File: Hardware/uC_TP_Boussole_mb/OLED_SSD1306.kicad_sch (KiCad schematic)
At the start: 2 parts, among them J6 Conn_01x04

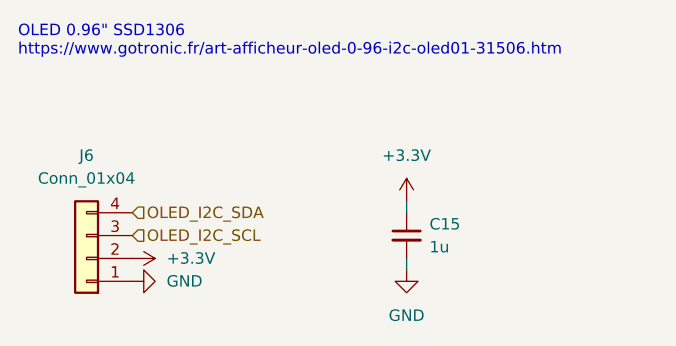
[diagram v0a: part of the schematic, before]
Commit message: starting pin out nucleo
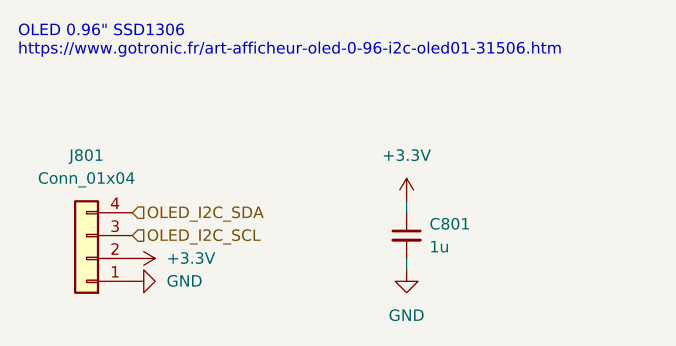
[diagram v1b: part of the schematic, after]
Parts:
- C801: renamed from C15; footprint (none) -> Capacitor_SMD:C_0402_1005Metric
- J801: renamed from J6; footprint (none) -> Connector_PinSocket_2.54mm:PinSocket_1x04_P2.54mm_Vertical
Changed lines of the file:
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@@
 		(dnp no)
 		(fields_autoplaced yes)
-		(property "Reference" "#PWR048"
+		(property "Reference" "#PWR0801"
 			(at 34.29 46.99 0)
 			(effects
@@
 			(project "uC_TP_Boussole_mb"
 				(path "/2e9feef3-d2ce-488a-99fa-e1de5099ffc3/51dbfd4b-530d-4bfc-b216-7850cc622368"
-					(reference "#PWR048")
+					(reference "#PWR0801")
 					(unit 1)
 				)
@@
 		(dnp no)
 		(fields_autoplaced yes)
-		(property "Reference" "#PWR051"
+		(property "Reference" "#PWR0804"
 			(at 68.58 54.61 0)
 			(effects
@@
 			(project "uC_TP_Boussole_mb"
 				(path "/2e9feef3-d2ce-488a-99fa-e1de5099ffc3/51dbfd4b-530d-4bfc-b216-7850cc622368"
-					(reference "#PWR051")
+					(reference "#PWR0804")
 					(unit 1)
 				)
@@
 		(dnp no)
 		(fields_autoplaced yes)
-		(property "Reference" "#PWR050"
+		(property "Reference" "#PWR0803"
 			(at 68.58 44.45 0)
 			(effects
@@
 			(project "uC_TP_Boussole_mb"
 				(path "/2e9feef3-d2ce-488a-99fa-e1de5099ffc3/51dbfd4b-530d-4bfc-b216-7850cc622368"
-					(reference "#PWR050")
+					(reference "#PWR0803")
 					(unit 1)
 				)
@@
 		(dnp no)
 		(fields_autoplaced yes)
-		(property "Reference" "C15"
+		(property "Reference" "C801"
 			(at 71.12 43.1862 0)
 			(effects
@@
 			)
 		)
-		(property "Footprint" ""
+		(property "Footprint" "Capacitor_SMD:C_0402_1005Metric"
 			(at 68.58 44.45 0)
 			(effects
@@
 			(project "uC_TP_Boussole_mb"
 				(path "/2e9feef3-d2ce-488a-99fa-e1de5099ffc3/51dbfd4b-530d-4bfc-b216-7850cc622368"
-					(reference "C15")
+					(reference "C801")
 					(unit 1)
 				)
@@
 		(dnp no)
 		(fields_autoplaced yes)
-		(property "Reference" "#PWR047"
+		(property "Reference" "#PWR0802"
 			(at 44.45 49.53 0)
 			(effects
@@
 			(project "uC_TP_Boussole_mb"
 				(path "/2e9feef3-d2ce-488a-99fa-e1de5099ffc3/51dbfd4b-530d-4bfc-b216-7850cc622368"
-					(reference "#PWR047")
+					(reference "#PWR0802")
 					(unit 1)
 				)
@@
 		(dnp no)
 		(fields_autoplaced yes)
-		(property "Reference" "J6"
+		(property "Reference" "J801"
 			(at 33.02 35.56 0)
 			(effects
@@
 			)
 		)
-		(property "Footprint" ""
+		(property "Footprint" "Connector_PinSocket_2.54mm:PinSocket_1x04_P2.54mm_Vertical"
 			(at 33.02 46.99 0)
 			(effects
@@
 			(project "uC_TP_Boussole_mb"
 				(path "/2e9feef3-d2ce-488a-99fa-e1de5099ffc3/51dbfd4b-530d-4bfc-b216-7850cc622368"
-					(reference "J6")
-					(unit 1)
-				)
+					(reference "J801")
+					(unit 1)
+				)

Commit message: ddd
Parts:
- added R801, R802: 1k, Resistor_SMD:R_0402_1005Metric, symbol Device:R_Small
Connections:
- net +3.3V: now also R801.2, R802.2
- net OLED_I2C_SCL: now also R801.1
- net OLED_I2C_SDA: now also R802.1
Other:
- note added: "Pull-up for I2C if it's not on OLED Screen"

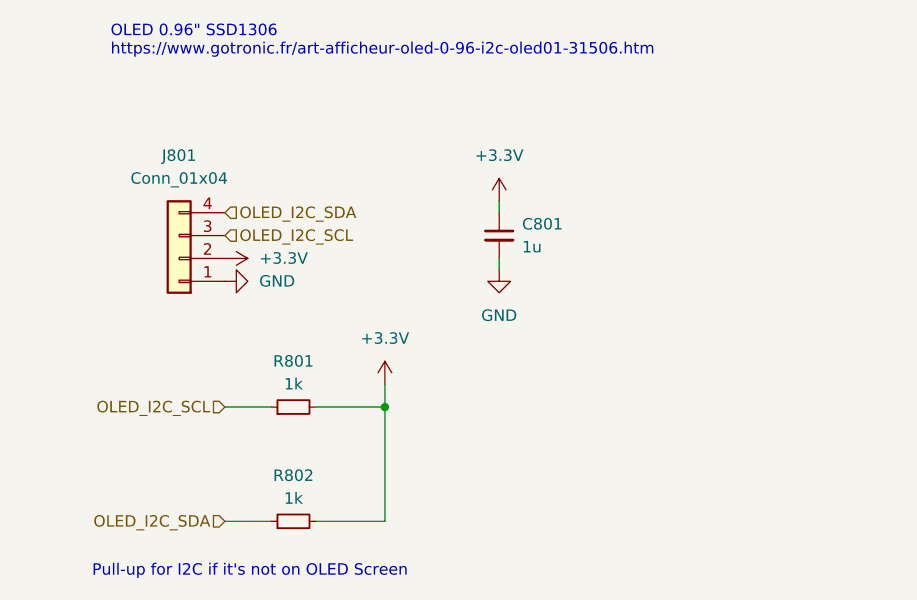
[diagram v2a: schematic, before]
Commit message: update schematic
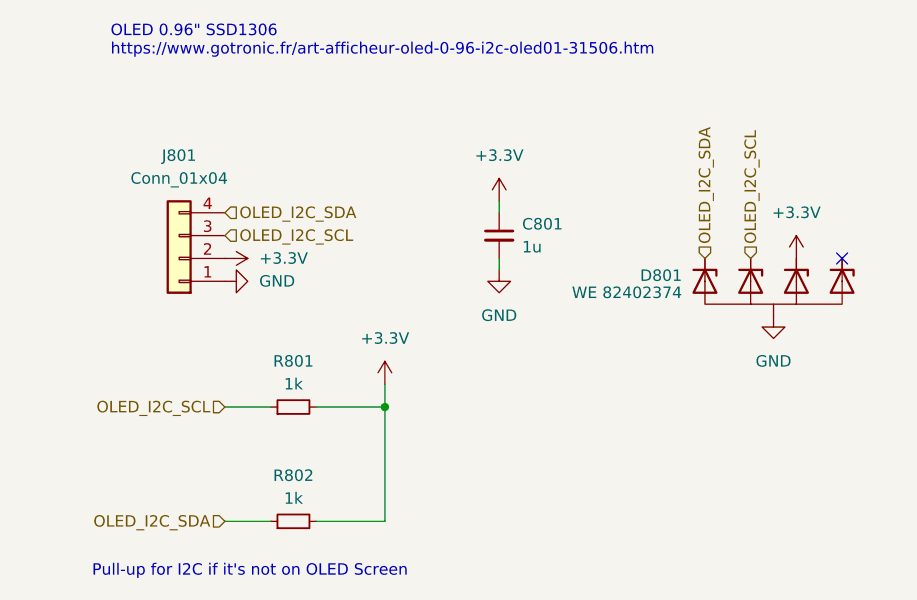
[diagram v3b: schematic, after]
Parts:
- added D801: WE 82402374, libs:SC70-5L, symbol mylibs:D_TVS_Uni_x4
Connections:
- net +3.3V: now also D801.3 (I/O)
- net GND: now also D801.2 (GND)
- net OLED_I2C_SCL: now also D801.4 (I/O)
- net OLED_I2C_SDA: now also D801.5 (I/O)
- no-connect marks 0 -> 1
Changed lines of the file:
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@@
 		(color 0 0 0 0)
+	)
+	(no_connect
+		(at 106.68 46.99)
 	)
 	(wire
@@
 	(hierarchical_label "OLED_I2C_SDA"
 		(shape input)
-		(at 38.1 76.2 180)
+		(at 91.44 46.99 90)
 		(fields_autoplaced yes)
 		(effects
@@
 				(size 1.27 1.27)
 			)
+			(justify left)
+		)
+	)
+	(hierarchical_label "OLED_I2C_SDA"
+		(shape input)
+		(at 38.1 76.2 180)
+		(fields_autoplaced yes)
+		(effects
+			(font
+				(size 1.27 1.27)
+			)
 			(justify right)
 		)
@@
 	(hierarchical_label "OLED_I2C_SCL"
 		(shape input)
-		(at 38.1 44.45 0)
+		(at 96.52 46.99 90)
 		(fields_autoplaced yes)
 		(effects
@@
 		)
 	)
+	(hierarchical_label "OLED_I2C_SCL"
+		(shape input)
+		(at 38.1 44.45 0)
+		(fields_autoplaced yes)
+		(effects
+			(font
+				(size 1.27 1.27)
+			)
+			(justify left)
+		)
+	)
 	(symbol
 		(lib_id "Device:R_Small")
@@
 	(symbol
 		(lib_id "power:+3.3V")
+		(at 101.6 46.99 0)
+		(unit 1)
+		(exclude_from_sim no)
+		(in_bom yes)
+		(on_board yes)
+		(dnp no)
+		(fields_autoplaced yes)
+		(property "Reference" "#PWR0807"
+			(at 101.6 50.8 0)
+			(effects
+				(font
+					(size 1.27 1.27)
+				)
+				(hide yes)
+			)
+		)
+		(property "Value" "+3.3V"
+			(at 101.6 41.91 0)
+			(effects
+				(font
+					(size 1.27 1.27)
+				)
+			)
+		)
+		(property "Footprint" ""
+			(at 101.6 46.99 0)
+			(effects
+				(font
+					(size 1.27 1.27)
+				)
+				(hide yes)
+			)
+		)
+		(property "Datasheet" ""
+			(at 101.6 46.99 0)
+			(effects
+				(font
+					(size 1.27 1.27)
+				)
+				(hide yes)
+			)
+		)
+		(property "Description" "Power symbol creates a global label with name \"+3.3V\""
+			(at 101.6 46.99 0)
+			(effects
+				(font
+					(size 1.27 1.27)
+				)
+				(hide yes)
+			)
+		)
+		(pin "1"
+		)
+		(instances
+			(project "uC_TP_Boussole_mb"
+				(path "/2e9feef3-d2ce-488a-99fa-e1de5099ffc3/51dbfd4b-530d-4bfc-b216-7850cc622368"
+					(reference "#PWR0807")
+					(unit 1)
+				)
+			)
+		)
+	)
+	(symbol
+		(lib_id "power:+3.3V")
 		(at 38.1 46.99 270)
 		(unit 1)
@@
 	)
 	(symbol
+		(lib_id "mylibs:D_TVS_Uni_x4")
+		(at 99.06 50.8 180)
+		(unit 1)
+		(exclude_from_sim no)
+		(in_bom yes)
+		(on_board yes)
+		(dnp no)
+		(fields_autoplaced yes)
+		(property "Reference" "D801"
+			(at 88.9 48.8949 0)
+			(effects
+				(font
+					(size 1.27 1.27)
+				)
+				(justify left)
+			)
+		)
+		(property "Value" "WE 82402374"
+			(at 88.9 50.8 0)
+			(effects
+				(font
+					(size 1.27 1.27)
+				)
+				(justify left)
+			)
+		)
+		(property "Footprint" "libs:SC70-5L"
+			(at 100.33 48.26 0)
+			(effects
+				(font
+					(size 1.27 1.27)
+				)
+				(hide yes)
+			)
+		)
+		(property "Datasheet" "https://www.we-online.com/components/products/datasheet/82402374.pdf"
+			(at 99.06 32.258 0)
+			(effects
+				(font
+					(size 1.27 1.27)
+				)
+				(hide yes)
+			)
+		)
+		(property "Description" "TVS 5V x4"
+			(at 99.314 34.29 0)
+			(effects
+				(font
+					(size 1.27 1.27)
+				)
+				(hide yes)
+			)
+		)
+		(property "MPN" "WE 82402374"
+			(at 98.806 37.084 0)
+			(effects
+				(font
+					(size 1.27 1.27)
+				)
+				(hide yes)
+			)
+		)
+		(pin "1"
+		)
+		(pin "2"
+		)
+		(pin "3"
+		)
+		(pin "4"
+		)
+		(pin "5"
+		)
+		(instances
+			(project "uC_TP_Boussole_mb"
+				(path "/2e9feef3-d2ce-488a-99fa-e1de5099ffc3/51dbfd4b-530d-4bfc-b216-7850cc622368"
+					(reference "D801")
+					(unit 1)
+				)
+			)
+		)
+	)
+	(symbol
 		(lib_id "power:+3.3V")
 		(at 55.88 60.96 0)
@@
 					(unit 1)
 				)
+			)
+		)
+	)
+	(symbol
+		(lib_id "power:GND")
+		(at 99.06 53.34 0)
+		(unit 1)
+		(exclude_from_sim no)
+		(in_bom yes)
+		(on_board yes)
+		(dnp no)
+		(fields_autoplaced yes)
+		(property "Reference" "#PWR0806"
+			(at 99.06 59.69 0)
+			(effects
+				(font
+					(size 1.27 1.27)
+				)
+				(hide yes)
+			)
+		)
+		(property "Value" "GND"
+			(at 99.06 58.42 0)
+			(effects
+				(font
+					(size 1.27 1.27)
+				)
+			)
+		)
+		(property "Footprint" ""
+			(at 99.06 53.34 0)
+			(effects
+				(font
+					(size 1.27 1.27)
+				)
+				(hide yes)
+			)
+		)
+		(property "Datasheet" ""
+			(at 99.06 53.34 0)
+			(effects
+				(font
+					(size 1.27 1.27)
+				)
+				(hide yes)
+			)
+		)
+		(property "Description" "Power symbol creates a global label with name \"GND\" , ground"
+			(at 99.06 53.34 0)
+			(effects
+				(font
+					(size 1.27 1.27)
+				)
+				(hide yes)
+			)
+		)
+		(pin "1"
+		)
+		(instances
+			(project "uC_TP_Boussole_mb"
+				(path "/2e9feef3-d2ce-488a-99fa-e1de5099ffc3/51dbfd4b-530d-4bfc-b216-7850cc622368"
+					(reference "#PWR0806")
+					(unit 1)
+				)

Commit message: finalize pcb
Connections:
- net +3.3V: now also D801.5 (I/O); no longer D801.3 (I/O)
- net OLED_I2C_SDA: now also D801.3 (I/O); no longer D801.5 (I/O)
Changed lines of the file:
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@@
 	(hierarchical_label "OLED_I2C_SDA"
 		(shape input)
-		(at 91.44 46.99 90)
+		(at 38.1 76.2 180)
 		(fields_autoplaced yes)
 		(effects
@@
 				(size 1.27 1.27)
 			)
-			(justify left)
+			(justify right)
 		)
 	)
 	(hierarchical_label "OLED_I2C_SDA"
 		(shape input)
-		(at 38.1 76.2 180)
+		(at 38.1 41.91 0)
 		(fields_autoplaced yes)
 		(effects
@@
 				(size 1.27 1.27)
 			)
-			(justify right)
+			(justify left)
 		)
 	)
 	(hierarchical_label "OLED_I2C_SDA"
 		(shape input)
-		(at 38.1 41.91 0)
+		(at 101.6 46.99 90)
 		(fields_autoplaced yes)
 		(effects
@@
 	(symbol
 		(lib_id "power:+3.3V")
-		(at 101.6 46.99 0)
-		(unit 1)
-		(exclude_from_sim no)
-		(in_bom yes)
-		(on_board yes)
-		(dnp no)
-		(fields_autoplaced yes)
-		(property "Reference" "#PWR0807"
-			(at 101.6 50.8 0)
-			(effects
-				(font
-					(size 1.27 1.27)
-				)
-				(hide yes)
-			)
-		)
-		(property "Value" "+3.3V"
-			(at 101.6 41.91 0)
-			(effects
-				(font
-					(size 1.27 1.27)
-				)
-			)
-		)
-		(property "Footprint" ""
-			(at 101.6 46.99 0)
-			(effects
-				(font
-					(size 1.27 1.27)
-				)
-				(hide yes)
-			)
-		)
-		(property "Datasheet" ""
-			(at 101.6 46.99 0)
-			(effects
-				(font
-					(size 1.27 1.27)
-				)
-				(hide yes)
-			)
-		)
-		(property "Description" "Power symbol creates a global label with name \"+3.3V\""
-			(at 101.6 46.99 0)
-			(effects
-				(font
-					(size 1.27 1.27)
-				)
-				(hide yes)
-			)
-		)
-		(pin "1"
-		)
-		(instances
-			(project "uC_TP_Boussole_mb"
-				(path "/2e9feef3-d2ce-488a-99fa-e1de5099ffc3/51dbfd4b-530d-4bfc-b216-7850cc622368"
-					(reference "#PWR0807")
-					(unit 1)
-				)
-			)
-		)
-	)
-	(symbol
-		(lib_id "power:+3.3V")
 		(at 38.1 46.99 270)
 		(unit 1)
@@
 					(unit 1)
 				)
+			)
+		)
+	)
+	(symbol
+		(lib_id "power:+3.3V")
+		(at 91.44 46.99 0)
+		(unit 1)
+		(exclude_from_sim no)
+		(in_bom yes)
+		(on_board yes)
+		(dnp no)
+		(fields_autoplaced yes)
+		(property "Reference" "#PWR0807"
+			(at 91.44 50.8 0)
+			(effects
+				(font
+					(size 1.27 1.27)
+				)
+				(hide yes)
+			)
+		)
+		(property "Value" "+3.3V"
+			(at 91.44 41.91 0)
+			(effects
+				(font
+					(size 1.27 1.27)
+				)
+			)
+		)
+		(property "Footprint" ""
+			(at 91.44 46.99 0)
+			(effects
+				(font
+					(size 1.27 1.27)
+				)
+				(hide yes)
+			)
+		)
+		(property "Datasheet" ""
+			(at 91.44 46.99 0)
+			(effects
+				(font
+					(size 1.27 1.27)
+				)
+				(hide yes)
+			)
+		)
+		(property "Description" "Power symbol creates a global label with name \"+3.3V\""
+			(at 91.44 46.99 0)
+			(effects
+				(font
+					(size 1.27 1.27)
+				)
+				(hide yes)
+			)
+		)
+		(pin "1"
+		)
+		(instances
+			(project "uC_TP_Boussole_mb"
+				(path "/2e9feef3-d2ce-488a-99fa-e1de5099ffc3/51dbfd4b-530d-4bfc-b216-7850cc622368"
+					(reference "#PWR0807")
+					(unit 1)
+				)

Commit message: change SBC01 footprint, add via GND, clean error and export gerbers
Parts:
- J801: footprint Connector_PinSocket_2.54mm:PinSocket_1x04_P2.54mm_Vertical -> libs:SBC-OLED01
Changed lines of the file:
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@@
 			)
 		)
-		(property "Footprint" "Connector_PinSocket_2.54mm:PinSocket_1x04_P2.54mm_Vertical"
+		(property "Footprint" "libs:SBC-OLED01"
 			(at 33.02 46.99 0)
 			(effects
